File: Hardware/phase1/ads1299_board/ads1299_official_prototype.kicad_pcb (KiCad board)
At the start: 4 copper layers, 88 parts, among them J6 36PIN_IDC, U1 ADS1299IPAG, U11 OPA376, U4 OPA376

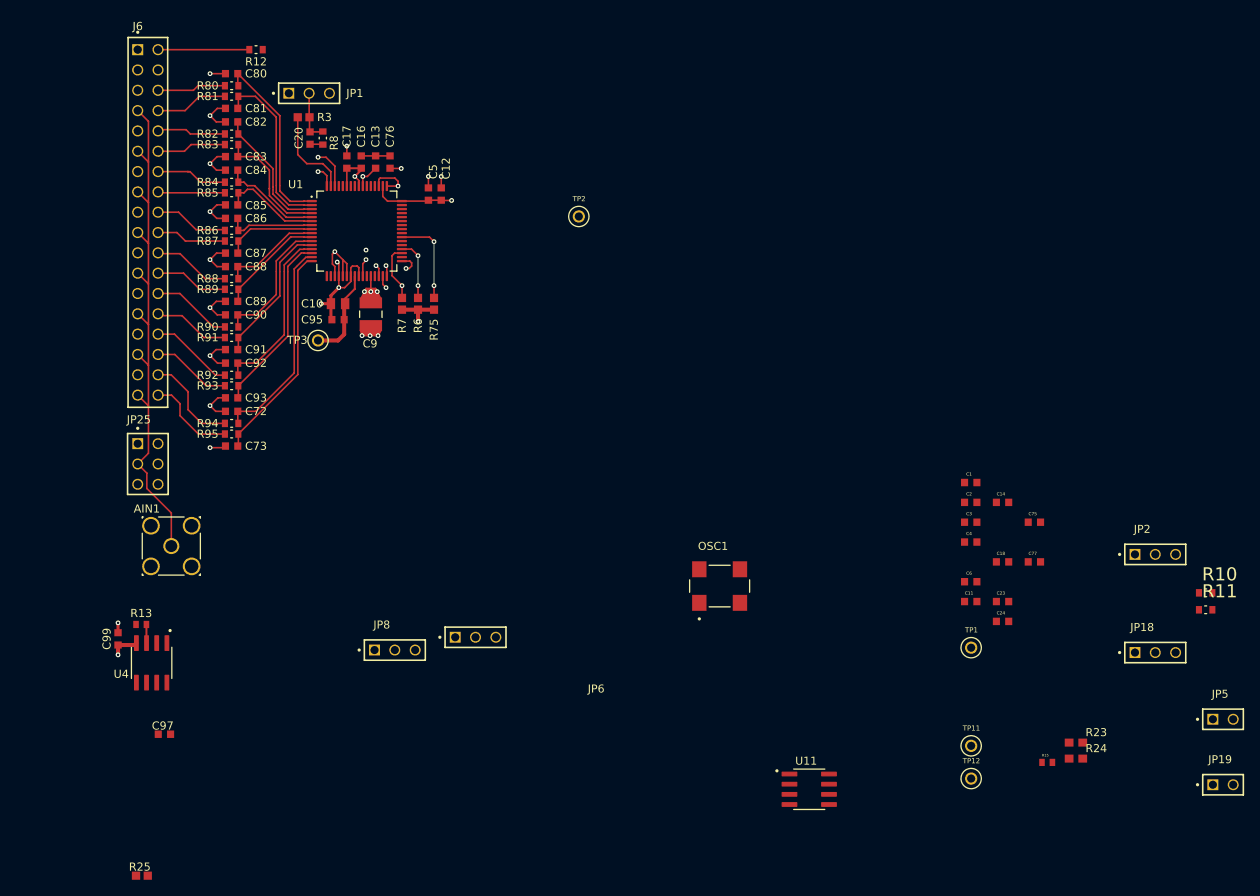
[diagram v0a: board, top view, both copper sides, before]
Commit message: ads1299 update (1.30.25)
- omit all NI components
- i still think it is a good idea to expose all pins for now, so i left off on implementing "Figure 62. ECG MDK Board Interface Adapter"
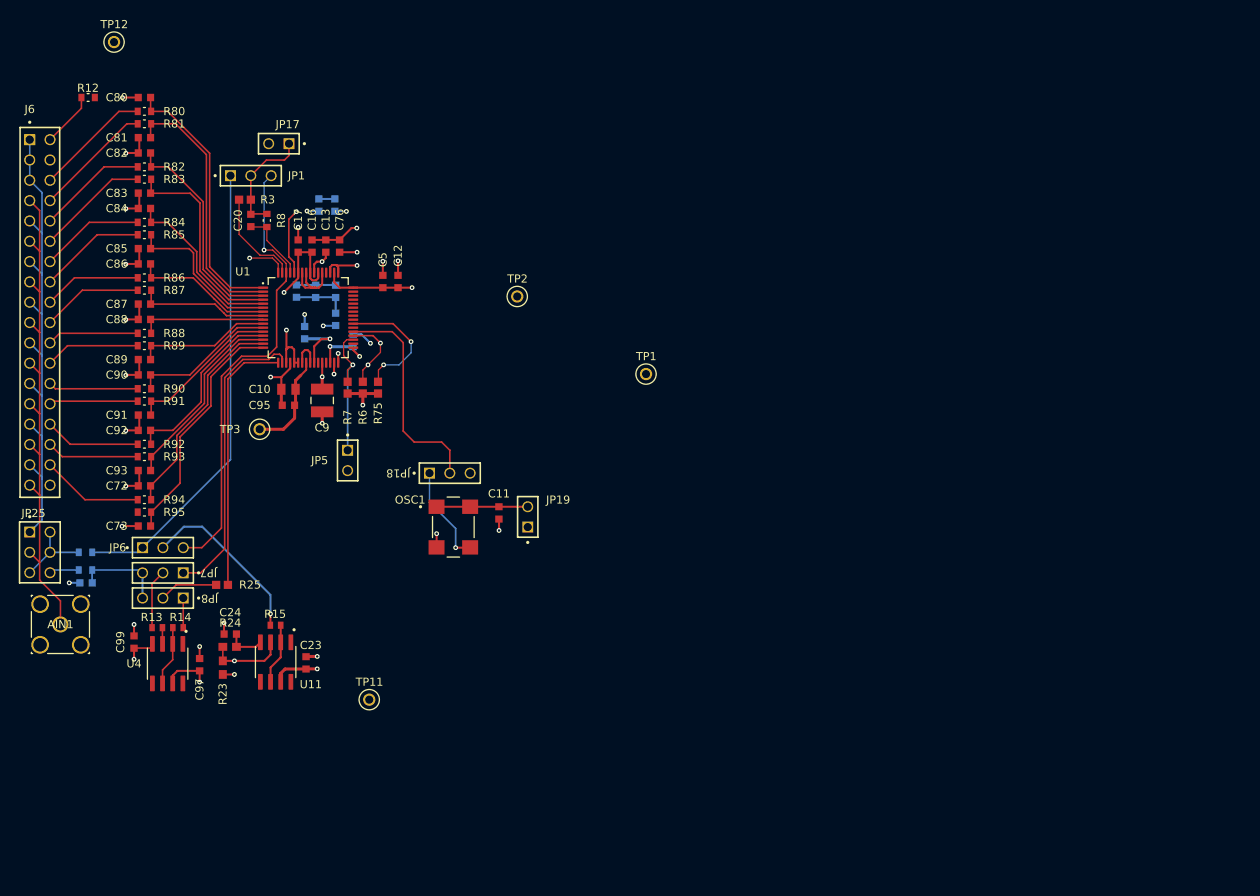
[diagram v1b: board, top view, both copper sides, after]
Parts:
- removed JP2: TSW-103-07-T-S, TSW-103-07-T-S:SAMTEC_TSW-103-07-T-S
- added JP17: TSW-102-07-T-S, TSW-102-07-T-S:SAMTEC_TSW-102-07-T-S, F.Cu at (123.1, 29.5)
- added JP7: TSW-103-07-T-S, TSW-103-07-T-S:SAMTEC_TSW-103-07-T-S, F.Cu at (108.6, 83.2)
- added R14: 0, RC0402JR-070RL:RESC1005X40, F.Cu at (110.5, 90.0)
- C1, C14, C18, C2, C3, C4, C6, C75, C77, R10, R11: moved to B.Cu
- moved TP12 141.3 mm to (102.5, 16.8)
- moved R11 140.1 mm to (98.9, 82.8)
- moved R10 140.1 mm to (98.9, 80.6)
- moved C75 118.8 mm to (99.0, 84.4), turned to 180 degrees
- moved JP5 114.1 mm to (131.7, 69.1), turned to -90 degrees
- moved R23 107.0 mm to (116.1, 95.0), turned to 90 degrees
- moved R24 106.7 mm to (117.0, 92.4), turned to 180 degrees
- moved C77 98.2 mm to (130.1, 37.2), turned to -90 degrees
- moved R15 98.0 mm to (122.7, 89.7), turned to 180 degrees
- moved C24 96.5 mm to (117.0, 90.8), turned to 180 degrees
- moved JP19 93.1 mm to (154.2, 76.2), turned to 90 degrees
- moved JP18 91.0 mm to (144.5, 70.7)
- moved C3 90.6 mm to (128.1, 37.2), turned to 90 degrees
- moved C4 89.9 mm to (125.3, 47.9), turned to 90 degrees
- moved C14 89.8 mm to (127.7, 48.0), turned to 90 degrees
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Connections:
- C2 pad 2: GNDA -> AVSS
- JP8 pad 01: Net-(U4--IN) -> Net-(JP8-Pad01)
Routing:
- net 1: track 0.00 -> 66.4 mm
- net BIAS_ELEC: track 0.00 -> 57.6 mm
- net BIASIN: track 5.06 -> 57.2 mm
- net SRB2: track 0.00 -> 37.1 mm
- net SRB1: track 0.00 -> 32.9 mm
- net CLK: track 0.00 -> 27.5 mm
- net AVDD: track 15.8 -> 40.3 mm, vias 2 -> 5
- net Net-(JP6-Pad02): track 0.00 -> 21.8 mm, vias 0 -> 1
- net AVSS: track 19.7 -> 38.0 mm, vias 4 -> 5
- net Net-(OSC1-OUTPUT): track 0.00 -> 12.5 mm, vias 0 -> 1
- net GNDA: track 51.9 -> 63.8 mm, vias 21 -> 27
- net Net-(OSC1-E/D): track 0.00 -> 11.4 mm
- net 36: track 11.3 -> 0.00 mm
- net REF_ELEC: track 0.00 -> 11.2 mm
- net AIN8P: track 21.9 -> 32.8 mm
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
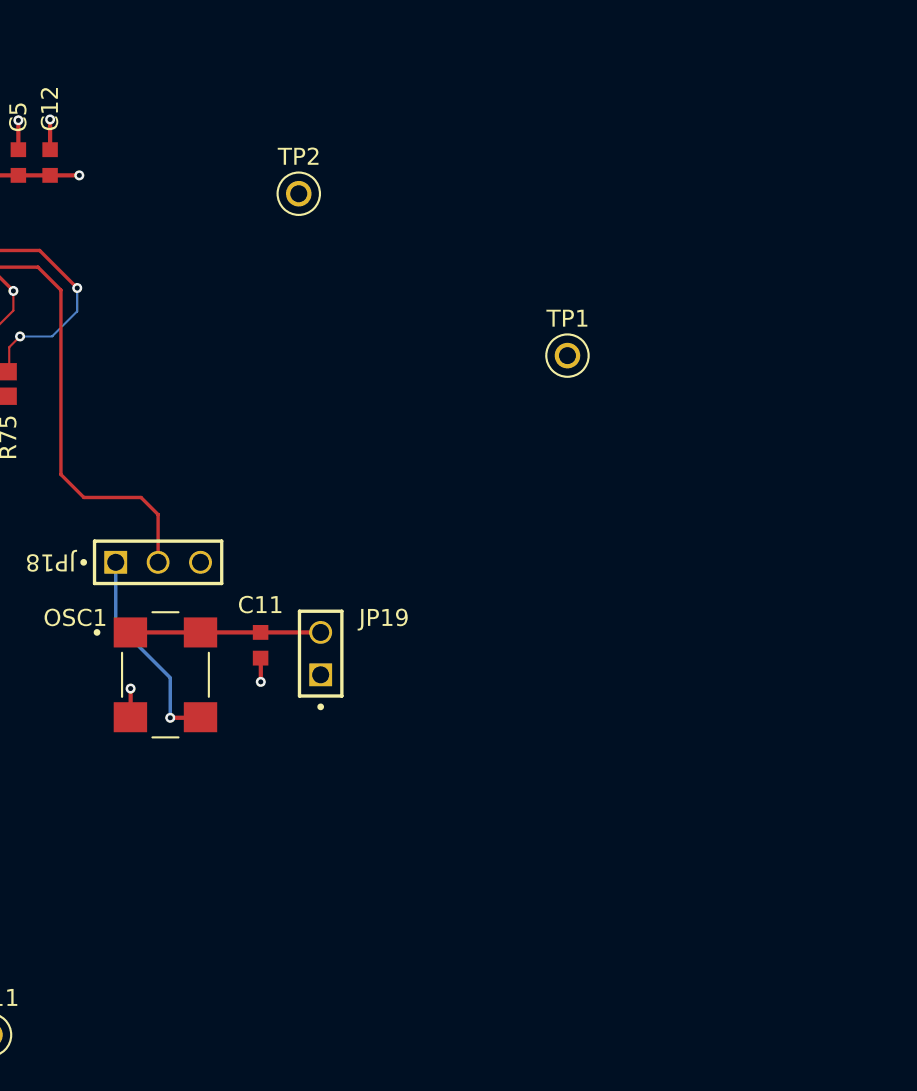
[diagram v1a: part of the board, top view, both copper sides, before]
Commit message: first update of the day (2.5.25)
- footprints need to be verified
- layout needs to be optimized
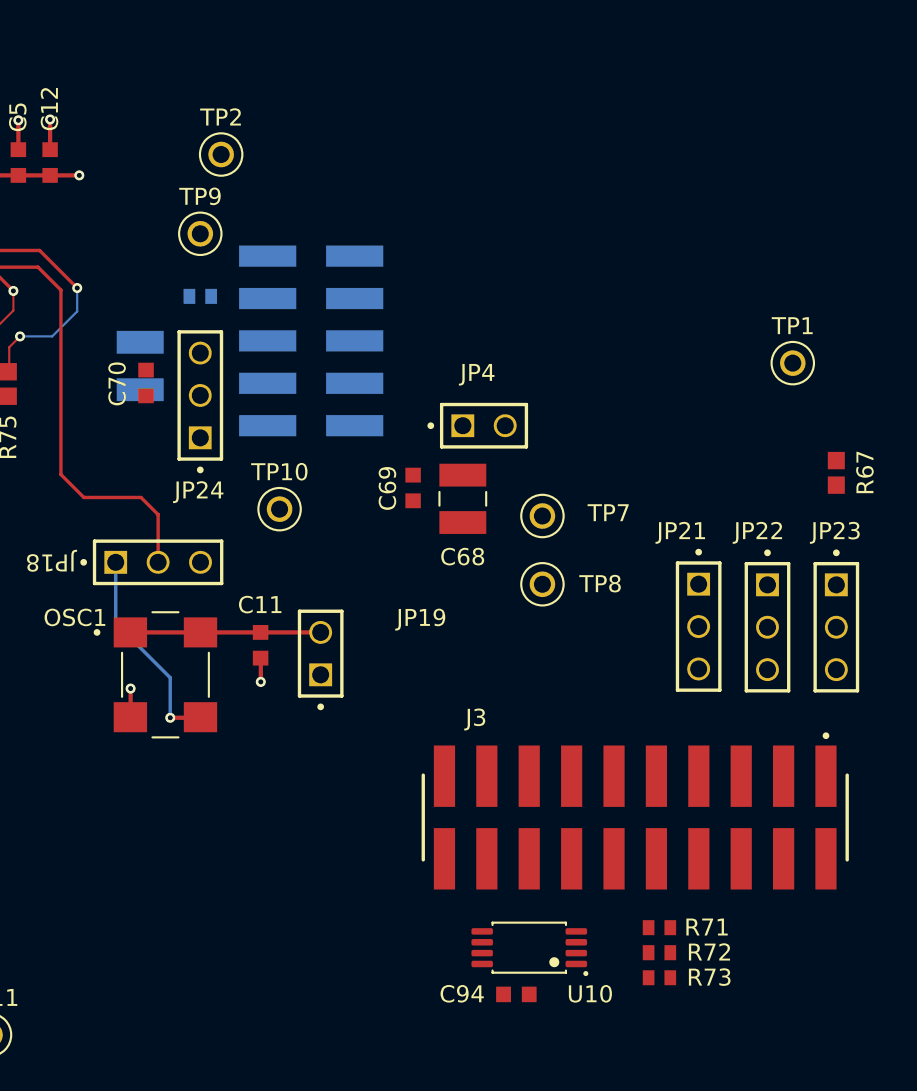
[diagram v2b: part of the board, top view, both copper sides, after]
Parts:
- added C68: 100uF, LMK325BJ107MM_T:CAPC3225X280N, F.Cu at (162.7, 66.9)
- added C69: 0.1uF, GRM188R71H104KA93D:CAPC1608X90N, F.Cu at (159.8, 66.2)
- added C70: 0.1uF, GRM188R71H104KA93D:CAPC1608X90N, F.Cu at (143.8, 59.9)
- added C71: 100uF, LMK325BJ107MM_T:CAPC3225X280N, B.Cu at (143.4, 58.9)
- added C94: 0.1uF, GRM188R71H104KA93D:CAPC1608X90N, F.Cu at (165.9, 96.6)
- added J3: Conn_02x10_Odd_Even, TSM-110-01-T-DV-P-TR:SAMTEC_TSM-110-01-T-DV-P-TR, F.Cu at (173.1, 86.0)
- added J4: ~, SSW-105-22-F-D-VS-K:SAMTEC_SSW-105-22-F-D-VS-K, B.Cu at (153.6, 57.4)
- added JP21: TSW-103-07-T-S, TSW-103-07-T-S:SAMTEC_TSW-103-07-T-S, F.Cu at (176.9, 74.5)
- added JP22: TSW-103-07-T-S, TSW-103-07-T-S:SAMTEC_TSW-103-07-T-S, F.Cu at (181.0, 74.6)
- added JP23: TSW-103-07-T-S, TSW-103-07-T-S:SAMTEC_TSW-103-07-T-S, F.Cu at (185.1, 74.6)
- added JP24: TSW-103-07-T-S, TSW-103-07-T-S:SAMTEC_TSW-103-07-T-S, F.Cu at (147.0, 60.7)
- added JP4: TSW-102-07-T-S, TSW-102-07-T-S:SAMTEC_TSW-102-07-T-S, F.Cu at (164.0, 62.5)
- added R67: 10K, RC0603FR-0710KL:RESC1607X60N, F.Cu at (185.1, 65.3)
- added R71: 0, RC0402JR-070RL:RESC1005X40, F.Cu at (174.5, 92.6)
- added R72: 0, RC0402JR-070RL:RESC1005X40, F.Cu at (174.5, 94.1)
- added R73: 0, RC0402JR-070RL:RESC1005X40, F.Cu at (174.5, 95.6)
- added R74: 0, RC0402JR-070RL:RESC1005X40, B.Cu at (147.0, 54.8)
- added TP10: 5001, 5001:KEYSTONE_5001, F.Cu at (151.8, 67.5)
- added TP7: 5001, 5001:KEYSTONE_5001, F.Cu at (167.5, 67.9)
- added TP8: 5001, 5001:KEYSTONE_5001, F.Cu at (167.5, 72.0)
- added TP9: 5001, 5001:KEYSTONE_5001, F.Cu at (147.0, 51.0)
- added U10: 24AA256-I/ST, 24AA256-I_ST:SOP8P65_300X640X120L60X24N, F.Cu at (166.7, 93.8)
- moved TP1 13.5 mm to (182.5, 58.8)
- moved TP2 5.21 mm to (148.2, 46.2)

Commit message: ads1299 2nd update (2.5.25)
- verified footprints
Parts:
- removed C20: 0.01uF, GRM188R71H103KA01D:CAPC1608X90N
- removed C23, C24: 1uF, GRM188R61E105KA12D:CAPC1608X90N
- removed JP1, JP6: TSW-103-07-T-S, TSW-103-07-T-S:SAMTEC_TSW-103-07-T-S
- removed JP17: TSW-102-07-T-S, TSW-102-07-T-S:SAMTEC_TSW-102-07-T-S
- removed R15: 0, RC0402JR-070RL:RESC1005X40
- removed R23, R24: 2M, RC0603JR-072ML:0603
- removed R3: 0, RC0603JR-070RL:RESC1607X60N
- removed R8: 392K, RC0603FR-07392KL:RESC1608X55N
- removed U11: OPA376, OPA376AID:SOIC127P599X175-8N
- added C15: 0.1uF, GRM188R71H104KA93D:CAPC1608X90N, B.Cu at (128.2, 47.9)
- added C19: 0.1uF, GRM188R71H104KA93D:CAPC1608X90N, B.Cu at (128.2, 51.2)
- added C25: 1uF, GRM188R61E105KA12D:CAPC1608X90N, F.Cu at (123.8, 42.2)
- added C26: 0.1uF, GRM188R71H104KA93D:CAPC1608X90N, F.Cu at (122.0, 42.2)
- added C7: 1uF, GRM188R61E105KA12D:CAPC1608X90N, B.Cu at (124.0, 37.2)
- added C8: 1uF, GRM188R61E105KA12D:CAPC1608X90N, B.Cu at (126.0, 37.2)
- added C98: 0.01uF, GRM188R71H104KA93D:CAPC1608X90N, F.Cu at (116.0, 86.2)
- added J3: Conn_02x10_Odd_Even, TSM-110-01-T-DV-P-TR:SAMTEC_TSM-110-01-T-DV-P-TR, B.Cu at (173.4, 89.7)
- added J5: ~, SSW-105-22-F-D-VS-K:SAMTEC_SSW-105-22-F-D-VS-K, F.Cu at (140.4, 89.8)
- added J5: ~, SSW-105-22-F-D-VS-K:SAMTEC_SSW-105-22-F-D-VS-K, B.Cu at (140.4, 89.8)
- TP10, TP7, TP9: footprint 5001:KEYSTONE_5001 -> 5000:KEYSTONE_5000
- moved TP2 4.25 mm to (150.2, 42.5)
- moved J3 3.82 mm to (173.4, 89.8)
- moved C94 3.79 mm to (166.3, 100.3)
- moved R71 3.79 mm to (174.8, 96.3)
- moved R72 3.79 mm to (174.8, 97.8)
- moved R73 3.79 mm to (174.8, 99.3)
- moved U10 3.79 mm to (167.0, 97.5)
- moved JP21 3.47 mm to (176.9, 78.0), turned to 90 degrees
- moved JP22 3.42 mm to (181.0, 78.0), turned to 90 degrees
- moved JP23 3.42 mm to (185.1, 78.0)
- moved C69 2.68 mm to (158.5, 68.6)
- moved C68 2.39 mm to (163.0, 69.2)
- moved JP4 2.27 mm to (161.7, 62.5), turned to 180 degrees
- moved JP7 1.90 mm to (108.6, 81.2)
- moved C14 1.45 mm to (126.2, 47.9)
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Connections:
- C9 pad 2: GNDA -> AVSS
- J4 pad 05: GND -> (no net)
- U1 pad 60: BIASREF -> unconnected-(U1-BIASREF-Pad60)
- U1 pad 61: BIASINV -> unconnected-(U1-BIASINV-Pad61)
- U1 pad 62: BIASIN -> unconnected-(U1-BIASIN-Pad62)
- U1 pad 63: BIASOUT -> unconnected-(U1-BIASOUT-Pad63)
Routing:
- net BIAS_ELEC: track 57.6 -> 0.00 mm
- net BIASIN: track 57.2 -> 0.00 mm, vias 1 -> 0
- net Net-(JP6-Pad02): track 21.8 -> 0.00 mm, vias 1 -> 0
- net AVDD: track 40.3 -> 25.9 mm, vias 5 -> 1
- net +5V: track 0.00 -> 14.4 mm
- net BIAS_DRV: track 14.1 -> 0.00 mm
- net BIASOUT: track 12.3 -> 0.00 mm
- net GND: track 0.00 -> 12.1 mm, vias 0 -> 1
- net REF_ELEC: track 11.2 -> 1.60 mm
- net AVSS: track 38.0 -> 28.4 mm, vias 5 -> 2
- net Net-(U11-+IN): track 9.52 -> 0.00 mm, vias 1 -> 0
- net BIASINV: track 8.93 -> 0.00 mm
- net BIASREF: track 8.29 -> 0.00 mm, vias 1 -> 0
- net Net-(J4-Pin_9): track 0.00 -> 7.84 mm
- net Net-(U11--IN): track 7.60 -> 0.00 mm
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
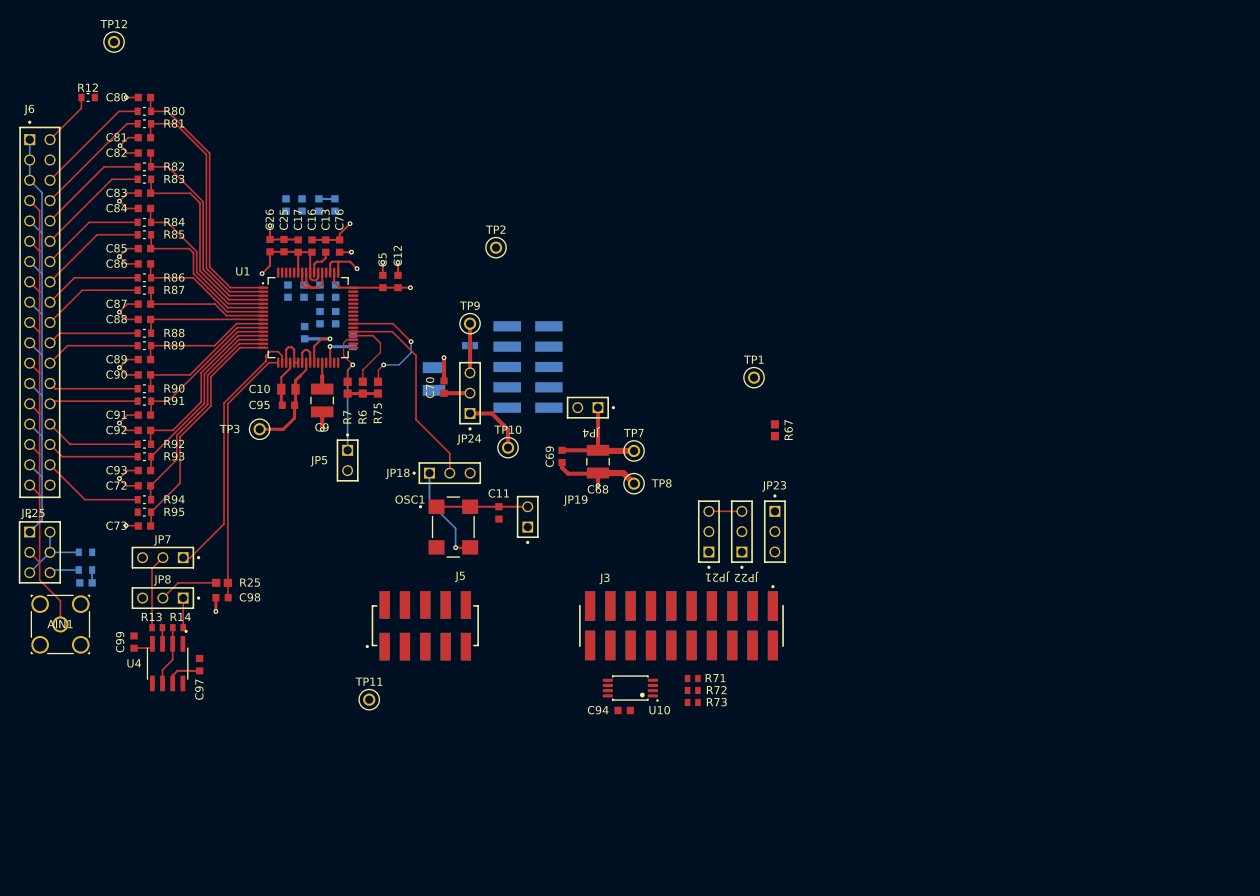
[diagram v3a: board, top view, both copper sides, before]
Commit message: ads1299 board 3rd update of today (2.5.25)
- still need to finish implementing barreljack and ECG power supply circuitry (both schematic/layout)
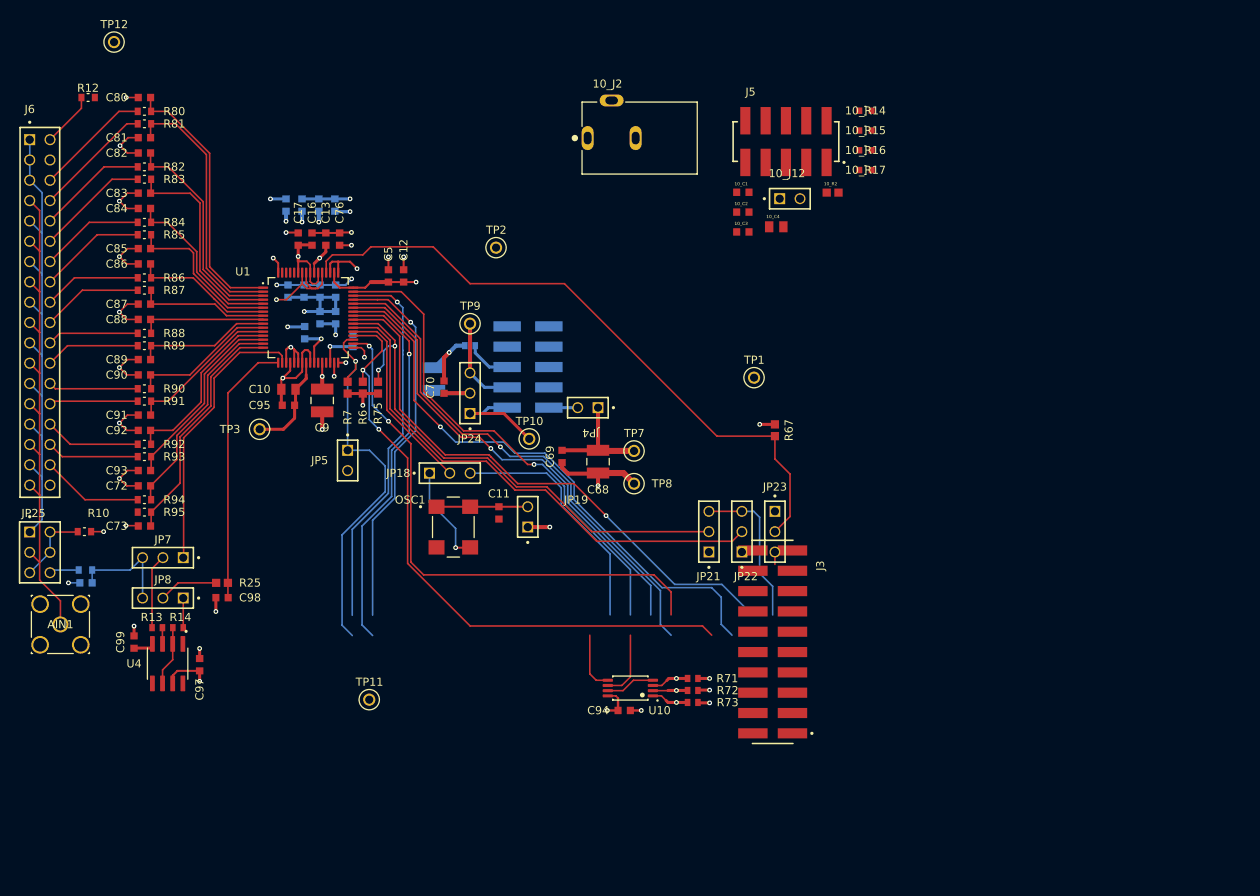
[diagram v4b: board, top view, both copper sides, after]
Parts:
- removed C25: 1uF, GRM188R61E105KA12D:CAPC1608X90N
- removed C26: 0.1uF, GRM188R71H104KA93D:CAPC1608X90N
- removed the J3 at (173.4, 89.7)
- removed the J5 at (140.4, 89.8) (x2)
- added 10_C1: 0.1uF, GRM188R71H104KA93D:CAPC1608X90N, F.Cu at (181.1, 35.6)
- added 10_C2: 0.01uF, GRM188R71H103KA01D:CAPC1608X90N, F.Cu at (181.1, 38.1)
- added 10_C3: 0.1uF, GRM188R71H104KA93D:CAPC1608X90N, F.Cu at (181.1, 40.5)
- added 10_C4: 10uF, GRM219R61A106KE44D:CAPC2012X95N, F.Cu at (185.3, 39.9)
- added 10_J12: TSW-102-07-T-S, TSW-102-07-T-S:SAMTEC_TSW-102-07-T-S, F.Cu at (187.0, 36.4)
- added 10_J2: PJ-102B, PJ_102B:CUI_PJ-102B, F.Cu at (168.2, 28.8)
- added 10_R14: 9.31K, RC0603FR-079K31L:RC0603N_YAG, F.Cu at (196.4, 25.4)
- added 10_R15: 51.1K, RC0603FR_0751K1L:RC0603N_YAG, F.Cu at (196.4, 27.9)
- added 10_R16: 30.1K, RC0603FR-0730K1L:RC0603N_YAG, F.Cu at (196.4, 30.3)
- added 10_R17: 30.1K, RC0603FR-0730K1L:RC0603N_YAG, F.Cu at (196.4, 32.8)
- added 10_R2: 10K, RC0603FR-0710KL:RESC1607X60N, F.Cu at (192.3, 35.6)
- added J5: ~, SSW-105-22-F-D-VS-K:SAMTEC_SSW-105-22-F-D-VS-K, F.Cu at (186.5, 29.2)
- R10: moved to F.Cu
- moved J3 11.6 mm to (184.8, 91.8), turned to -90 degrees
- moved TP10 2.87 mm to (154.4, 66.4)
- moved R10 2.59 mm to (98.8, 78.0)
- moved C5 0.99 mm to (136.8, 46.0)
- moved C12 0.99 mm to (138.7, 46.0)
- moved C13 0.87 mm to (129.0, 41.4)
- moved C16 0.87 mm to (127.2, 41.4)
- moved C17 0.87 mm to (125.5, 41.4)
- moved C76 0.87 mm to (130.7, 41.4)
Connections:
- net +3V3 renamed /MR2
- R10 pad 2: BIAS_ELEC -> GNDA
- U1 pad 17: SRB1 -> unconnected-(U1-SRB1-Pad17)
- U1 pad 18: SRB2 -> unconnected-(U1-SRB2-Pad18)
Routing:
- net CLKSEL: track 0.00 -> 81.6 mm
- net GPIO1: track 0.00 -> 71.7 mm, vias 0 -> 1
- net SPI_CLK: track 0.00 -> 70.5 mm, vias 0 -> 1
- net /RESET: track 9.53 -> 78.2 mm, vias 0 -> 2
- net SPI_IN: track 0.00 -> 68.2 mm, vias 0 -> 2
- net SPI_START: track 0.00 -> 65.2 mm
- net GPIO2: track 0.00 -> 64.6 mm, vias 0 -> 1
- net SPI_DRDY: track 0.00 -> 61.6 mm, vias 0 -> 1
- net SPI_OUT: track 0.00 -> 60.4 mm, vias 0 -> 1
- net SPI_CS: track 16.0 -> 66.0 mm
- net DAISY_IN: track 0.00 -> 48.1 mm, vias 0 -> 1
- net GPIO4: track 0.00 -> 47.9 mm, vias 0 -> 1
- net GPIO3: track 0.00 -> 47.5 mm, vias 0 -> 1
- net EXT_CLK: track 0.00 -> 30.6 mm
- net /PWDN: track 17.9 -> 48.3 mm
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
